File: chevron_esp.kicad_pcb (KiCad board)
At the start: 2 copper layers, 20 parts, among them J1 282837-4, K1 SRD-05VDC-SL-C, K2 SRD-05VDC-SL-C, K3 SRD-05VDC-SL-C, P1 282837-2, Q1 PN2222A, Q2 PN2222A, Q3 PN2222A, SW1 1825057-2, U1 ESP32-DEVKIT-V1, U2 RA-02_LORA

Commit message: chevron esp v1.0
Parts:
- removed R11, R13, R15: 330, Resistor_SMD:R_1206_3216Metric
- removed R12, R14, R16: 10k, Resistor_SMD:R_1206_3216Metric
- added R1: 330, Resistor_SMD:R_1206_3216Metric, F.Cu at (174.5, 90.0)
- added R2: 10k, Resistor_SMD:R_1206_3216Metric, F.Cu at (166.0, 90.0)
- added R3: 330, Resistor_SMD:R_1206_3216Metric, F.Cu at (157.5, 90.0)
- added R4: 10k, Resistor_SMD:R_1206_3216Metric, F.Cu at (175.0, 81.5)
- added R5: 330, Resistor_SMD:R_1206_3216Metric, F.Cu at (166.0, 81.5)
- added R6: 10k, Resistor_SMD:R_1206_3216Metric, F.Cu at (157.0, 81.0)
- moved Q1 141.8 mm to (116.0, 98.5)
- moved Q3 136.0 mm to (126.0, 98.4)
- moved Q2 134.9 mm to (106.0, 98.5)
- moved SW1 86.3 mm to (143.3, 66.5)
- moved U2 75.0 mm to (161.8, 122.7), turned to 90 degrees
- moved K2 71.6 mm to (95.5, 74.5)
- moved D15 68.8 mm to (91.5, 105.5)
- moved P1 68.3 mm to (91.0, 123.5)
- moved D14 67.1 mm to (91.5, 99.5)
- moved D13 65.8 mm to (91.5, 94.0)
- moved K1 51.8 mm to (123.5, 74.5)
- moved K3 46.0 mm to (118.5, 117.0)
- moved J1 38.4 mm to (180.2, 66.0), turned to 180 degrees
- moved U1 31.7 mm to (61.8, 93.5), turned to 180 degrees
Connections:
- K1 pad NC: GND -> unconnected-(K1-PadNC)
- K1 pad NO: unconnected-(K1-PadNO) -> GND
- K2 pad NC: GND -> unconnected-(K2-PadNC)
- K2 pad NO: unconnected-(K2-PadNO) -> GND
- K3 pad NC: GND -> unconnected-(K3-PadNC)
- K3 pad NO: unconnected-(K3-PadNO) -> GND
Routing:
- net GND: track 0.00 -> 233.8 mm
- net +5V: track 0.00 -> 156.5 mm
- net Net-(U1-D23): track 0.00 -> 139.3 mm, vias 0 -> 1
- net Net-(U1-D13): track 0.00 -> 134.1 mm, vias 0 -> 1
- net Net-(U1-D12): track 0.00 -> 131.8 mm, vias 0 -> 1
- net Net-(U1-D19): track 0.00 -> 126.9 mm, vias 0 -> 1
- net Net-(U1-D5): track 0.00 -> 114.5 mm, vias 0 -> 1
- net Net-(U1-D26): track 0.00 -> 114.0 mm, vias 0 -> 1
- net Net-(U1-D14): track 0.00 -> 112.9 mm, vias 0 -> 1
- net Net-(U1-D18): track 0.00 -> 108.8 mm
- net Net-(U1-D15): track 0.00 -> 99.5 mm, vias 0 -> 1
- net Net-(J1-Pad4): track 0.00 -> 92.0 mm, vias 0 -> 1
- net Net-(J1-Pad3): track 0.00 -> 86.2 mm
- net Net-(U1-3V3): track 0.00 -> 83.1 mm, vias 0 -> 1
- net Net-(Q2-B): track 0.00 -> 80.6 mm, vias 0 -> 1
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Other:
- board outline added: 150 x 70 mm
- board text added: "+12v"
- board text added: "G1"
- board text added: "G2"
- board text added: "G3"

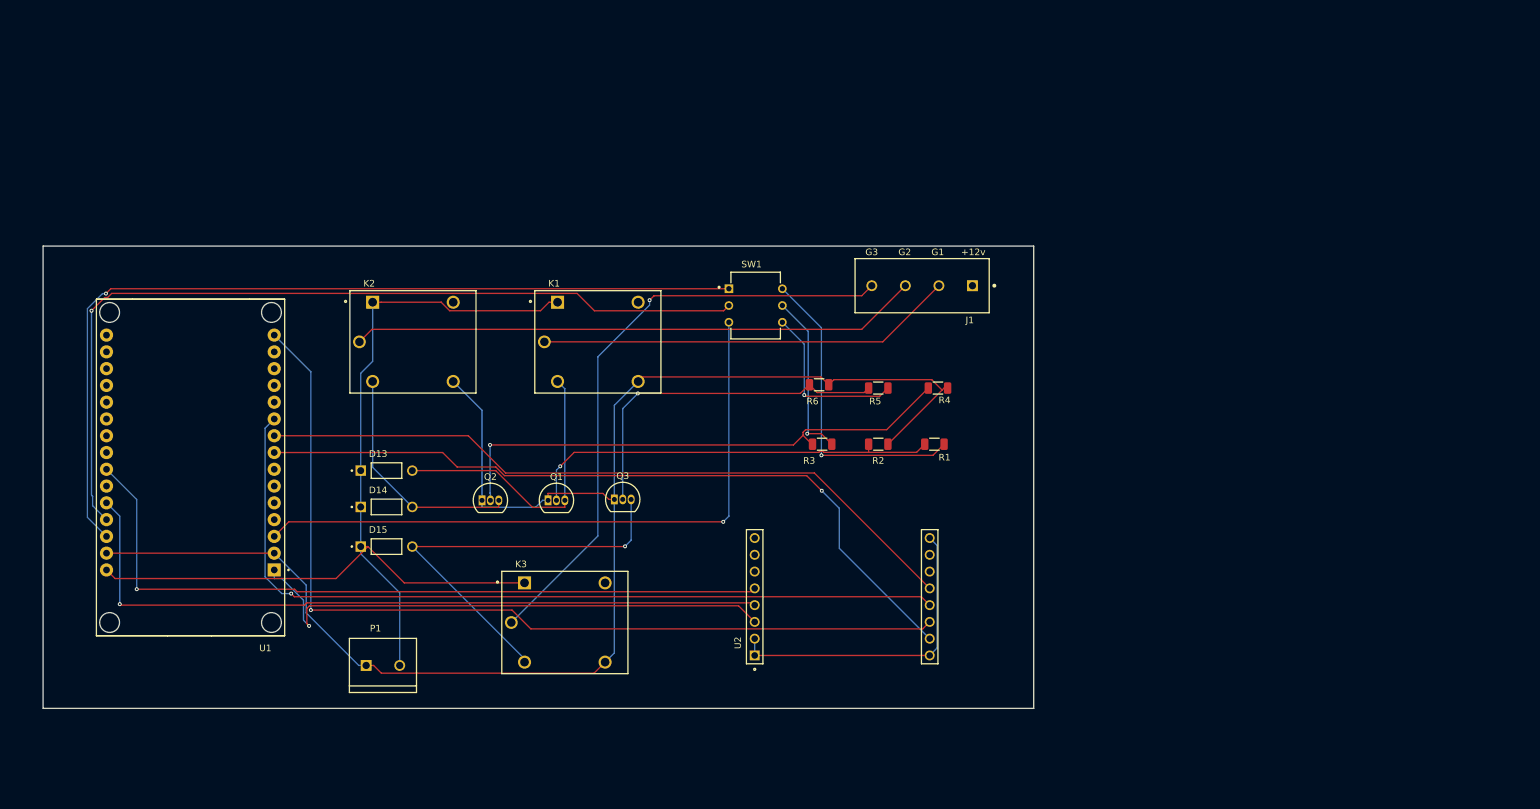
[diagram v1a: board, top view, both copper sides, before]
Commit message: chevron esp v1.1
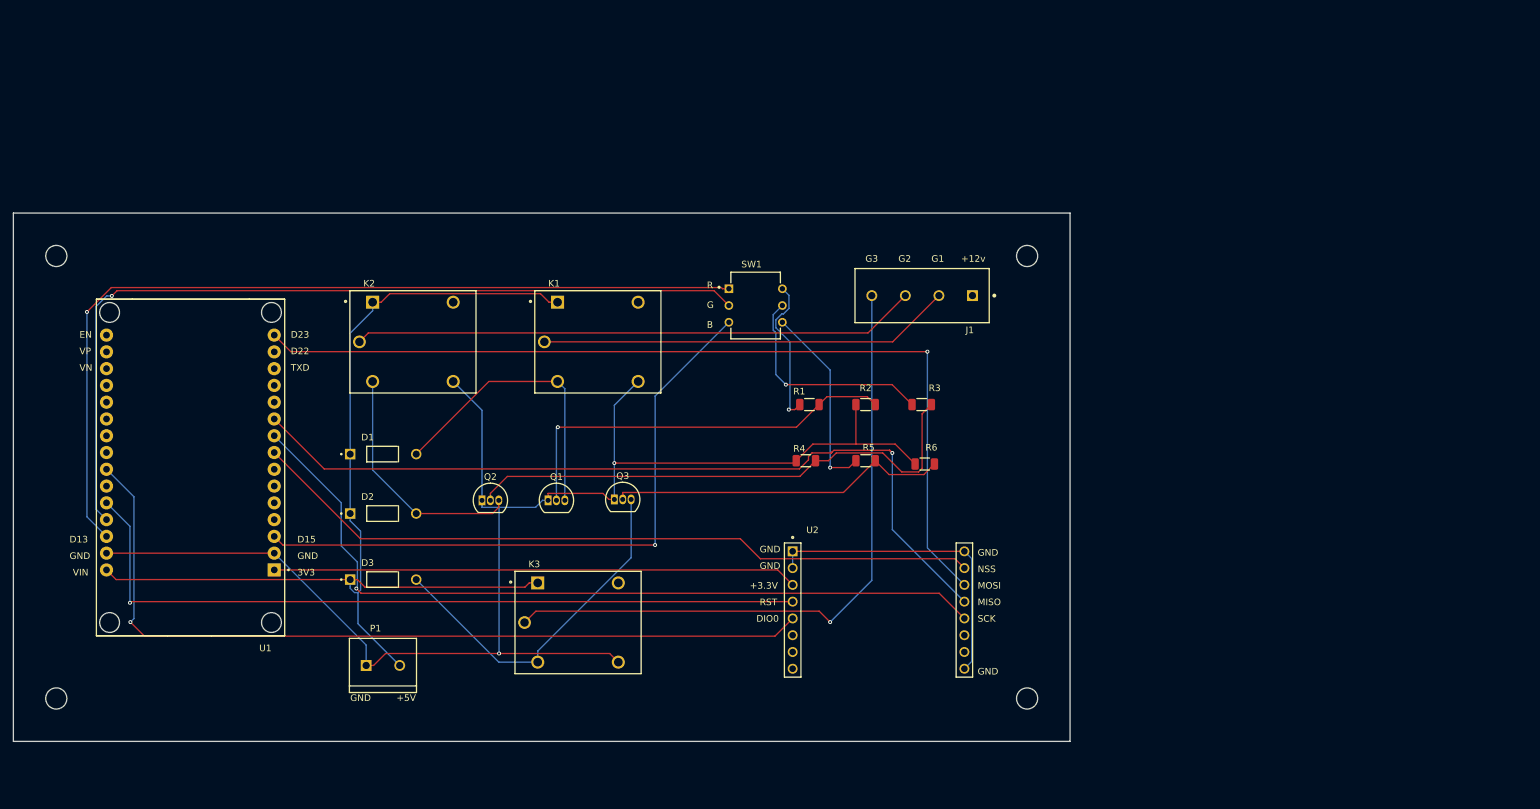
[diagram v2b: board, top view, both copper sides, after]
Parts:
- removed D13, D14, D15: 1N4007-T, 1N4007-T:DIOAD780W78L463D236
- added D1: 1N4007-T, 1N4007-T:DIOAD780W78L463D236, F.Cu at (91.0, 91.5)
- added D2: 1N4007-T, 1N4007-T:DIOAD780W78L463D236, F.Cu at (91.0, 100.5)
- added D3: 1N4007-T, 1N4007-T:DIOAD780W78L463D236, F.Cu at (91.0, 110.5)
- added ~: MountingHole_3.2mm_M3, MountingHole:MountingHole_3.2mm_M3, F.Cu at (41.5, 61.5)
- added ~: MountingHole_3.2mm_M3, MountingHole:MountingHole_3.2mm_M3, F.Cu at (41.5, 128.5)
- added ~: MountingHole_3.2mm_M3, MountingHole:MountingHole_3.2mm_M3, F.Cu at (188.5, 61.5)
- added ~: MountingHole_3.2mm_M3, MountingHole:MountingHole_3.2mm_M3, F.Cu at (188.5, 128.5)
- moved R4 22.8 mm to (155.0, 92.5), turned to 0 degrees
- moved R6 20.0 mm to (173.0, 93.0), turned to 0 degrees
- moved R1 19.9 mm to (155.5, 84.0), turned to 0 degrees
- moved R3 16.2 mm to (172.5, 84.0), turned to 0 degrees
- moved R5 11.2 mm to (164.0, 92.5), turned to 0 degrees
- moved U2 7.43 mm to (157.0, 117.0), turned to 0 degrees
- moved R2 6.30 mm to (164.0, 84.0), turned to 0 degrees
- moved K3 2.00 mm to (120.5, 117.0)
- moved J1 1.50 mm to (180.2, 67.5)
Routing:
- net Net-(R1-Pad1): track 46.9 -> 22.6 mm
- net Net-(U1-D18): track 108.8 -> 122.4 mm, vias 0 -> 1
- net Net-(U1-D26): track 114.0 -> 127.3 mm
- net Net-(Q3-C): track 64.3 -> 54.1 mm, vias 1 -> 0
- net Net-(R3-Pad1): track 25.5 -> 33.9 mm
- net Net-(J1-Pad4): track 92.0 -> 99.7 mm
- net GND: track 233.8 -> 226.4 mm, vias 0 -> 2
- net Net-(U1-D14): track 112.9 -> 117.0 mm
- net Net-(R5-Pad1): track 25.7 -> 29.3 mm
- net Net-(U1-3V3): track 83.1 -> 79.4 mm, vias 1 -> 0
- net Net-(U1-D15): track 99.5 -> 96.6 mm
- net Net-(U1-D5): track 114.5 -> 111.7 mm, vias 1 -> 0
- net +5V: track 156.5 -> 158.3 mm
- net Net-(U1-D23): track 139.3 -> 137.6 mm
- net Net-(Q3-B): track 53.3 -> 51.8 mm, vias 1 -> 0
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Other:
- board size 150 x 70 mm -> 160 x 80 mm
- board text added: "+3.3V"
- board text added: "+5V"
- board text added: "3V3"
- board text added: "B"
- board text added: "D13"
- board text added: "D15"
- board text added: "D22"
- board text added: "D23"
- board text added: "DIO0"
- board text added: "EN"
- board text added: "G"
- board text added: "GND"
- board text added: "MISO"
- board text added: "MOSI"
- board text added: "NSS"
- board text added: "R"
- board text added: "RST"
- board text added: "SCK"
- board text added: "TXD"
- board text added: "VIN"
- board text added: "VN"
- board text added: "VP"

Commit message: chevron esp v1.2
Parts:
- removed ~ (x4): MountingHole_3.2mm_M3, MountingHole:MountingHole_3.2mm_M3
- added H1: MountingHole_3.2mm_M3, MountingHole:MountingHole_3.2mm_M3, F.Cu at (228.8, 62.5)
- added H2: MountingHole_3.2mm_M3, MountingHole:MountingHole_3.2mm_M3, F.Cu at (228.8, 129.5)
- added H3: MountingHole_3.2mm_M3, MountingHole:MountingHole_3.2mm_M3, F.Cu at (71.8, 129.5)
- added H4: MountingHole_3.2mm_M3, MountingHole:MountingHole_3.2mm_M3, F.Cu at (71.8, 62.5)
- added J2: MTSW-101-09-G-S-104x4, MTSW-101-09-G-S-104:SAMTEC_MTSW-101-09-G-S-104x4, F.Cu at (76.8, 111.5)
- moved D3 137.9 mm to (224.8, 77.0), turned to 90 degrees
- moved D2 126.0 mm to (214.8, 77.0), turned to 90 degrees
- moved U1 118.5 mm to (180.3, 93.5)
- moved D1 115.7 mm to (205.8, 77.0), turned to 90 degrees
- moved J1 94.5 mm to (102.6, 121.5), turned to 0 degrees
- moved U2 62.1 mm to (219.1, 115.0), turned to 90 degrees
- moved SW1 53.3 mm to (152.8, 118.9)
- moved K3 45.5 mm to (113.8, 72.0)
- moved K1 44.8 mm to (134.3, 118.0)
- moved R6 37.3 mm to (146.3, 67.0), turned to 90 degrees
- moved Q2 30.2 mm to (134.8, 89.5), turned to 90 degrees
- moved K2 27.8 mm to (114.3, 95.0)
- moved Q3 25.6 mm to (134.8, 74.3), turned to 90 degrees
- moved R5 25.3 mm to (146.3, 74.5), turned to 90 degrees
- moved R1 23.6 mm to (148.3, 106.5), turned to 90 degrees
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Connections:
- J1 pad 1: unconnected-(J1-Pad1) -> +12V
- P1 pad 1: GND -> +12V
- P1 pad 2: +5V -> GND
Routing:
- net Net-(U1-D23): track 137.6 -> 28.5 mm, vias 1 -> 0
- net Net-(U1-D13): track 134.0 -> 29.8 mm
- net Net-(U1-D19): track 126.8 -> 27.1 mm
- net Net-(U1-D18): track 122.4 -> 28.0 mm
- net Net-(U1-D12): track 130.7 -> 36.4 mm, vias 1 -> 0
- net Net-(U1-D5): track 111.7 -> 19.6 mm
- net Net-(Q2-C): track 36.7 -> 126.1 mm, vias 0 -> 1
- net GND: track 226.4 -> 312.2 mm, vias 2 -> 0
- net Net-(Q1-C): track 44.4 -> 124.9 mm, vias 0 -> 1
- net Net-(Q3-C): track 54.1 -> 126.4 mm
- net +5V: track 158.3 -> 220.0 mm, vias 0 -> 2
- net Net-(J1-Pad3): track 85.6 -> 29.2 mm
- net Net-(U1-3V3): track 79.4 -> 24.5 mm
- net Net-(U1-D26): track 127.3 -> 74.9 mm
- net Net-(Q2-B): track 80.6 -> 29.2 mm
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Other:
- board size 160 x 80 mm -> 170 x 80 mm
- board text added: "+12V"
- board text added: "IN"
- board text added: "OUT"
- board text removed: "+5V"

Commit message: v1 ok
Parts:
- removed D1, D2, D3: 1N4007-T, 1N4007-T:DIOAD780W78L463D236
- removed J1: 282837-4, 282837-4:TE_282837-4
- removed K1, K2, K3: SRD-05VDC-SL-C, SRD-05VDC-SL-C:RELAY_SRD-05VDC-SL-C
- removed Q1, Q2, Q3: PN2222A, Package_TO_SOT_THT:TO-92_Inline
- added C1: 0.1uF, Capacitor_SMD:C_0603_1608Metric_Pad1.08x0.95mm_HandSolder, F.Cu at (227.8, 70.8)
- added C2: 1uF, Capacitor_SMD:C_1206_3216Metric_Pad1.33x1.80mm_HandSolder, F.Cu at (223.3, 70.0)
- added C3: 10uF, Capacitor_SMD:C_0805_2012Metric_Pad1.18x1.45mm_HandSolder, F.Cu at (219.3, 70.2)
- added J3: Conn_02x05_Counter_Clockwise, Connector_IDC:IDC-Header_2x05_P2.54mm_Vertical, F.Cu at (186.6, 67.2)
- added R7: 100, Resistor_SMD:R_1206_3216Metric_Pad1.30x1.75mm_HandSolder, F.Cu at (181.7, 88.8)
- added R8: 100, Resistor_SMD:R_1206_3216Metric_Pad1.30x1.75mm_HandSolder, F.Cu at (181.8, 93.8)
- H1: renamed from H4; value MountingHole_3.2mm_M3 -> 3.2mm_M3_TH; footprint MountingHole:MountingHole_3.2mm_M3 -> Mounting Hole:3.2mm_M3_TH
- H2: renamed from H1; value MountingHole_3.2mm_M3 -> 3.2mm_M3_TH; footprint MountingHole:MountingHole_3.2mm_M3 -> Mounting Hole:3.2mm_M3_TH
- H3: renamed from H2; value MountingHole_3.2mm_M3 -> 3.2mm_M3_TH; footprint MountingHole:MountingHole_3.2mm_M3 -> Mounting Hole:3.2mm_M3_TH
- H4: renamed from H3; value MountingHole_3.2mm_M3 -> 3.2mm_M3_TH; footprint MountingHole:MountingHole_3.2mm_M3 -> Mounting Hole:3.2mm_M3_TH
- P1: footprint 282837-2:TE_282837-2 -> Connector_PinHeader_2.54mm:PinHeader_1x02_P2.54mm_Vertical
- R1, R3: value 330 -> 10K; footprint Resistor_SMD:R_1206_3216Metric -> Resistor_SMD:R_1206_3216Metric_Pad1.30x1.75mm_HandSolder
- R2, R4: value 10k -> 10K; footprint Resistor_SMD:R_1206_3216Metric -> Resistor_SMD:R_1206_3216Metric_Pad1.30x1.75mm_HandSolder
- R5: value 330 -> 100; footprint Resistor_SMD:R_1206_3216Metric -> Resistor_SMD:R_1206_3216Metric_Pad1.30x1.75mm_HandSolder
- R6: value 10k -> 100; footprint Resistor_SMD:R_1206_3216Metric -> Resistor_SMD:R_1206_3216Metric_Pad1.30x1.75mm_HandSolder
- SW1: value 1825057-2 -> SW_DIP_x04; footprint 1825057-2:DIP810W60P254L1010H480Q6 -> Button_Switch_THT:SW_DIP_SPSTx04_Slide_6.7x11.72mm_W7.62mm_P2.54mm_LowProfile
- moved P1 71.5 mm to (129.7, 65.5)
- moved R6 43.0 mm to (181.7, 91.3), turned to 0 degrees
- moved J2 39.6 mm to (103.0, 81.7), turned to -90 degrees
- moved R5 37.4 mm to (181.8, 86.2), turned to 0 degrees
- moved U2 36.9 mm to (222.2, 78.2), turned to -90 degrees
- moved SW1 36.2 mm to (134.1, 88.0), turned to 180 degrees
- moved R4 28.6 mm to (132.2, 98.6), turned to -90 degrees
- moved H4 23.9 mm to (83.1, 108.5)
- moved R1 22.7 mm to (127.1, 98.6), turned to -90 degrees
- moved R3 22.2 mm to (134.7, 98.6), turned to -90 degrees
- moved U1 21.9 mm to (160.8, 83.6)
- moved H3 21.2 mm to (228.8, 108.3)
- moved R2 18.7 mm to (129.6, 98.6), turned to -90 degrees
- moved H1 11.4 mm to (83.2, 62.6)
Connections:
- H1 pad : (no net) -> GND
- H2 pad : (no net) -> GND
- H3 pad : (no net) -> GND
- H4 pad : (no net) -> GND
- R1 pad 1: Net-(R1-Pad1) -> Net-(U1-D25)
- R1 pad 2: Net-(Q1-B) -> VDD_3V3
- R2 pad 1: GND -> Net-(U1-D26)
- R2 pad 2: Net-(Q1-B) -> VDD_3V3
- R3 pad 1: Net-(R3-Pad1) -> Net-(U1-D12)
- R3 pad 2: Net-(Q2-B) -> VDD_3V3
- R4 pad 1: GND -> Net-(U1-D14)
- R4 pad 2: Net-(Q2-B) -> VDD_3V3
- R5 pad 1: Net-(R5-Pad1) -> Net-(U1-D2)
- R5 pad 2: Net-(Q3-B) -> CLK
- R6 pad 1: GND -> Net-(U1-D4)
- R6 pad 2: Net-(Q3-B) -> OE
- SW1 pad 1: Net-(U1-D13) -> Net-(U1-D12)
- SW1 pad 2: Net-(U1-D12) -> Net-(U1-D14)
- SW1 pad 3: Net-(U1-D15) -> Net-(U1-D26)
- SW1 pad 4: Net-(R5-Pad1) -> Net-(U1-D25)
- SW1 pad 5: Net-(R3-Pad1) -> GND
- SW1 pad 6: Net-(R1-Pad1) -> GND
- U1 pad 1: Net-(U1-3V3) -> VDD_3V3
- U1 pad 10: Net-(U1-D19) -> unconnected-(U1-D19-Pad10)
- U1 pad 21: unconnected-(U1-D32-Pad21) -> Net-(U1-D32)
- U1 pad 22: unconnected-(U1-D33-Pad22) -> Net-(U1-D33)
- U1 pad 23: unconnected-(U1-D25-Pad23) -> Net-(U1-D25)
- U1 pad 25: unconnected-(U1-D27-Pad25) -> Net-(U1-D27)
- U1 pad 28: Net-(U1-D13) -> unconnected-(U1-D13-Pad28)
- U1 pad 3: Net-(U1-D15) -> unconnected-(U1-D15-Pad3)
- U1 pad 4: unconnected-(U1-D2-Pad4) -> Net-(U1-D2)
- U1 pad 5: unconnected-(U1-D4-Pad5) -> Net-(U1-D4)
- U1 pad 6: unconnected-(U1-RX2-Pad6) -> Net-(U1-RX2)
- U1 pad 7: unconnected-(U1-TX2-Pad7) -> Net-(U1-TX2)
- U1 pad 9: Net-(U1-D18) -> unconnected-(U1-D18-Pad9)
- U2 pad 1: Net-(U2-GND-Pad1) -> GND
- U2 pad 12: Net-(U1-D18) -> Net-(U1-TX2)
- U2 pad 13: Net-(U1-D19) -> Net-(U1-RX2)
- U2 pad 14: Net-(U1-D23) -> Net-(U1-D27)
- U2 pad 15: Net-(U1-D5) -> Net-(U1-D33)
- U2 pad 16: Net-(U2-GND-Pad1) -> GND
- U2 pad 2: Net-(U2-GND-Pad1) -> GND
- U2 pad 3: Net-(U1-3V3) -> VDD_3V3
- U2 pad 4: Net-(U1-D14) -> Net-(U1-D32)
- U2 pad 5: Net-(U1-D26) -> unconnected-(U2-DI00-Pad5)
- U2 pad 9: Net-(U2-GND-Pad1) -> GND
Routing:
- net GND: track 312.2 -> 67.9 mm, vias 0 -> 25
- net +5V: track 220.0 -> 41.5 mm, vias 2 -> 0
- net Net-(Q3-C): track 126.4 -> 0.00 mm
- net Net-(Q2-C): track 126.1 -> 0.00 mm, vias 1 -> 0
- net Net-(Q1-C): track 124.9 -> 0.00 mm, vias 1 -> 0
- net Net-(U1-D32): track 0.00 -> 116.2 mm, vias 0 -> 4
- net VDD_3V3: track 0.00 -> 115.7 mm, vias 0 -> 2
- net Net-(U1-D33): track 0.00 -> 104.5 mm, vias 0 -> 2
- net Net-(U1-D27): track 0.00 -> 96.0 mm, vias 0 -> 2
- net Net-(U1-RX2): track 0.00 -> 73.4 mm, vias 0 -> 2
- net Net-(U1-TX2): track 0.00 -> 63.2 mm, vias 0 -> 1
- net Net-(R5-Pad1): track 55.9 -> 0.00 mm, vias 1 -> 0
- net Net-(U1-D15): track 55.4 -> 0.00 mm, vias 1 -> 0
- net Net-(J1-Pad4): track 54.5 -> 0.00 mm
- net Net-(U2-GND-Pad1): track 47.4 -> 0.00 mm
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- added copper zone on B.Cu, net GND
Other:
- board size 170 x 80 mm -> 158.8 x 59.1 mm
- board text added: "1"
- board text added: "2"
- board text added: "3"
- board text added: "3v3"
- board text added: "4"
- board text added: "CLK"
- board text added: "LE"
- board text added: "OE"
- board text added: "POWER"
- board text added: "SDO"
- board text removed: "+12v"
- board text removed: "+3.3V"
- board text removed: "3V3"
- board text removed: "B"
- board text removed: "D13"
- board text removed: "D15"
- board text removed: "DIO0"
- board text removed: "G"
- board text removed: "G1"
- board text removed: "G2"
- board text removed: "G3"
- board text removed: "IN"
- board text removed: "R"
- board text removed: "TXD"
- board text removed: "VN"

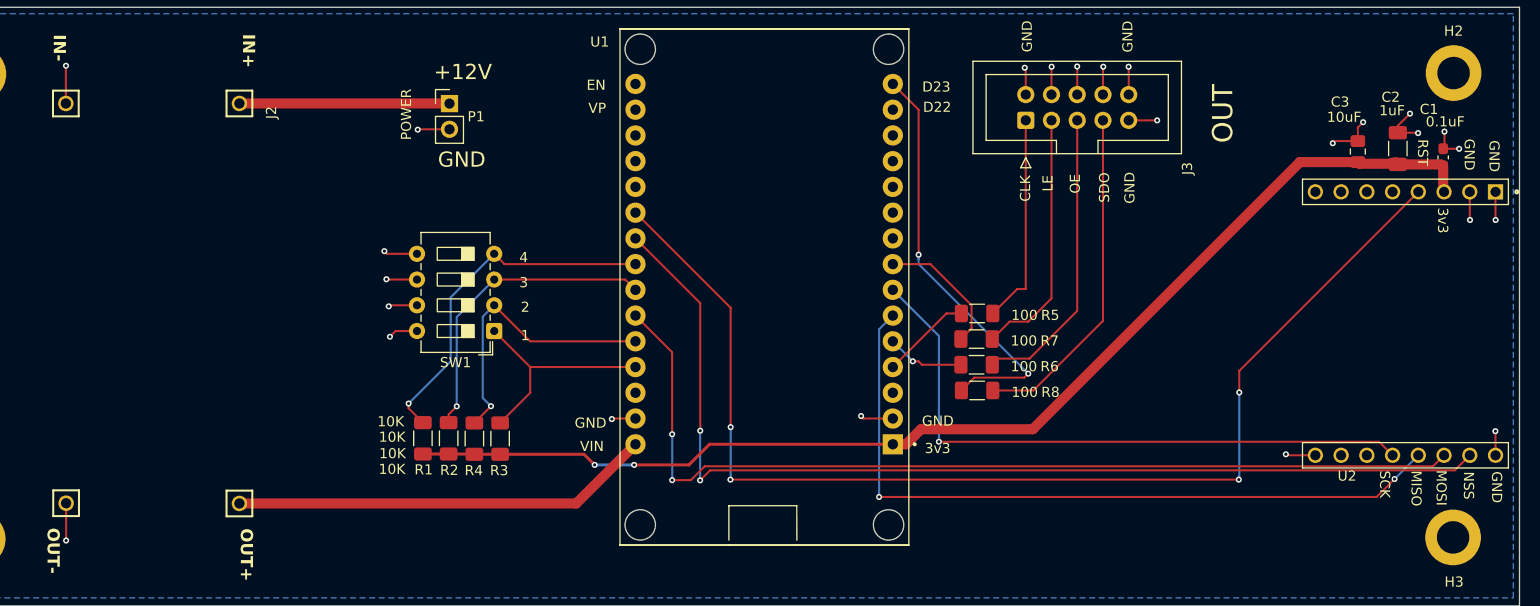
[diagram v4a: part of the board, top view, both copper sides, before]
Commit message: cleanup tracks and vias
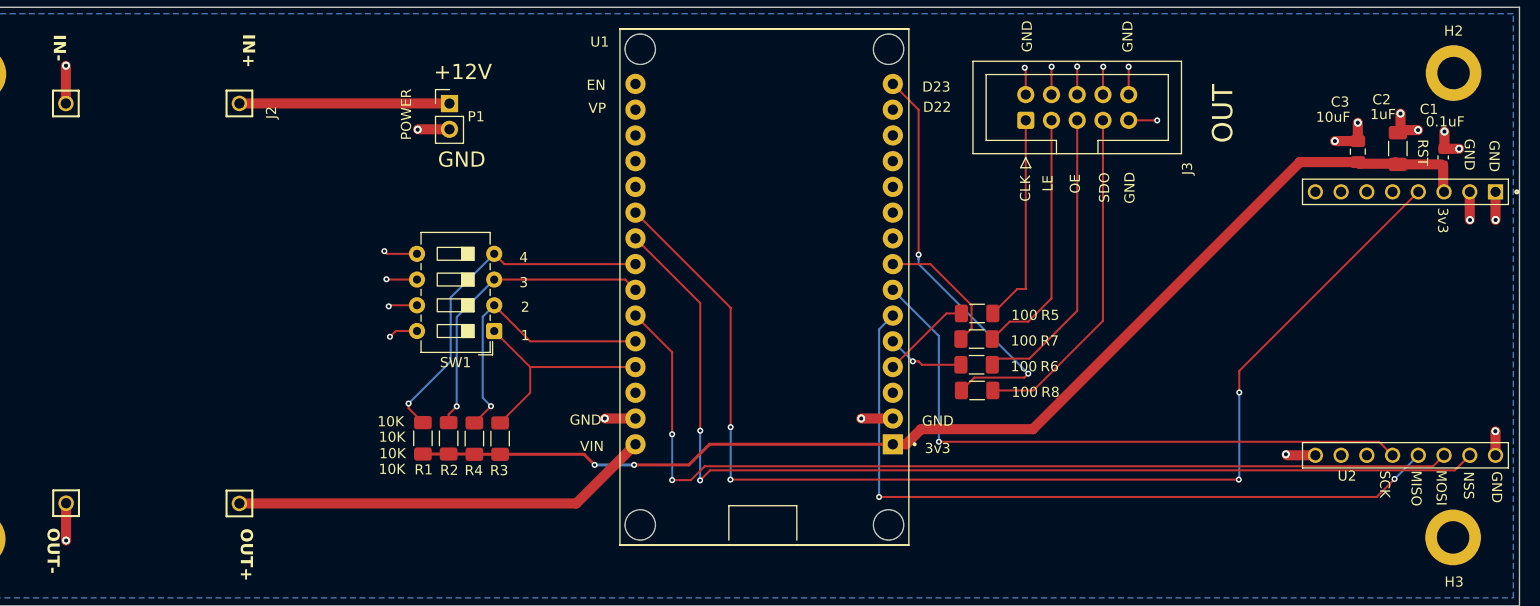
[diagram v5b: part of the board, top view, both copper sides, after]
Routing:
- net GND: track 67.9 -> 66.8 mm
